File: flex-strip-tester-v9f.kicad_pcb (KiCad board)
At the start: 2 copper layers, 68.8 x 11.1 mm, 12 parts, among them J2 Conn_01x01_Female

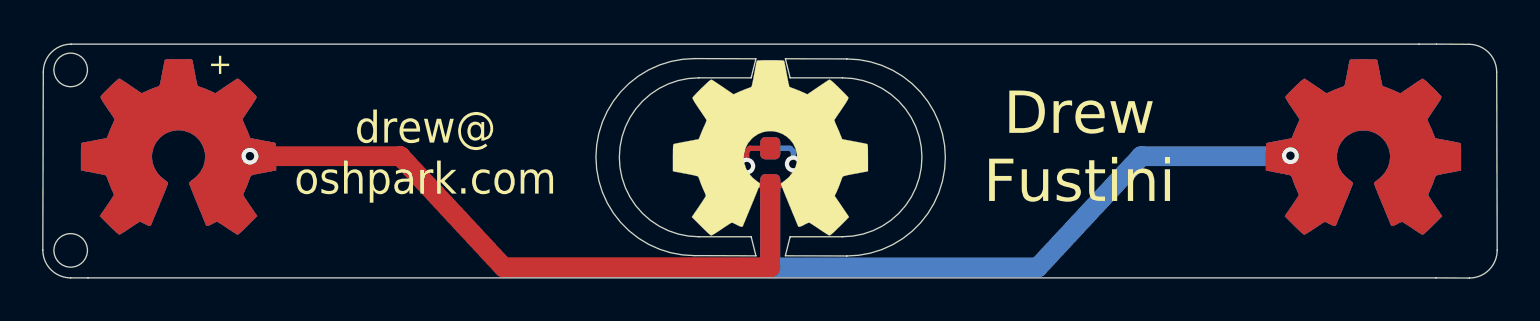
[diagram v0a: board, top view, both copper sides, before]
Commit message: add v10 which is being order from oshpark flex
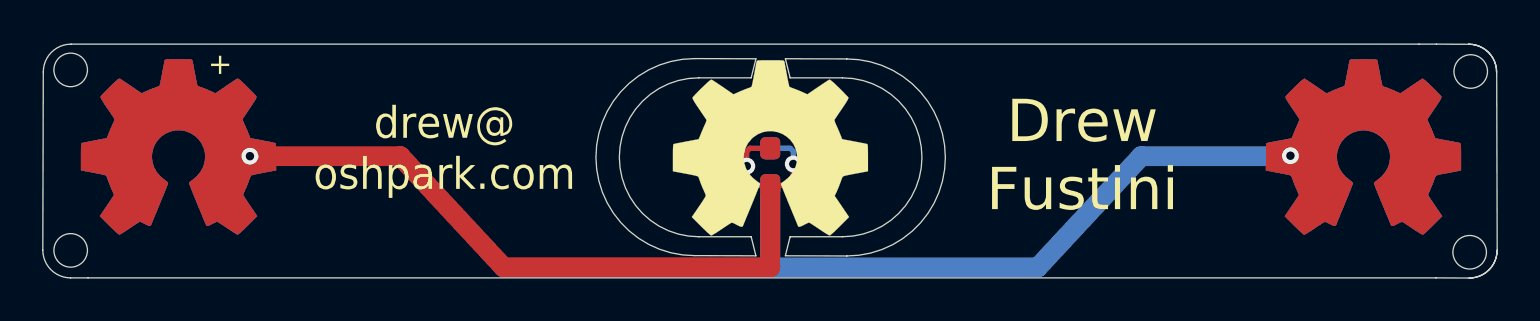
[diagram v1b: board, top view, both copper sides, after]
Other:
- outline, holes or cut-outs redrawn
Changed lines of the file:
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@@
-(kicad_pcb (version 20200628) (host pcbnew "(5.99.0-2143-g1463dd10b)")
+(kicad_pcb (version 20200628) (host pcbnew "(5.99.0-2281-g2f31bf278-dirty)")
   (general
     (thickness 0.1)
-    (drawings 85)
+    (drawings 89)
     (tracks 24)
     (modules 12)
@@
     )
   )
+  (gr_arc (start 186.273635 99.979326) (end 186.273635 101.29404) (angle -90) (layer "Edge.Cuts") (width 0.05))
+  (gr_circle (center 186.293095 100.075) (end 186.883095 100.605) (layer "Edge.Cuts") (width 0.05))
+  (gr_arc (start 186.247423 91.54446) (end 187.562137 91.54446) (angle -90) (layer "Edge.Cuts") (width 0.05))
+  (gr_circle (center 186.343097 91.525) (end 186.873097 90.935) (layer "Edge.Cuts") (width 0.05))
   (gr_line (start 152.5325 90.924712) (end 149.625 90.914904) (layer "Edge.Cuts") (width 0.05))
   (gr_line (start 152.3075 91.825096) (end 149.83 91.825096) (layer "Edge.Cuts") (width 0.05))
@@
   (gr_line (start 153.23 95.43) (end 187.57 95.43) (layer "F.Fab") (width 0.1))
   (gr_line (start 146.06 100.83) (end 186.9286 100.83) (layer "B.Fab") (width 0.1))
-  (gr_text "Drew\nFustini" (at 167.83558 95.11284) (layer "F.SilkS")
+  (gr_text "Drew\nFustini" (at 167.975 95.5) (layer "F.SilkS")
     (effects (font (size 2 2) (thickness 0.3)))
   )
@@
   (gr_line (start 155.2575 99.06) (end 154.6225 99.06) (layer "Eco1.User") (width 0.1))
   (gr_line (start 154.6225 99.06) (end 154.6225 98.3615) (layer "Eco1.User") (width 0.1))
-  (gr_text "drew@\noshpark.com" (at 136.9 95.4) (layer "F.SilkS")
+  (gr_text "drew@\noshpark.com" (at 137.8 95.175) (layer "F.SilkS")
     (effects (font (size 1.5 1.4) (thickness 0.2)))
   )
-  (gr_text "github.com/\noshpark/\nflextester" (at 136.4 95.5) (layer "B.SilkS")
+  (gr_text "github.com/\noshpark/\nflextester" (at 137.625 95.3) (layer "B.SilkS")
     (effects (font (size 1.5 1.5) (thickness 0.2286)) (justify mirror))
   )
@@
     (effects (font (size 1 1) (thickness 0.15)))
   )
-  (gr_text "Flex\nbattery \ntester" (at 168.00322 95.76054) (layer "B.SilkS")
+  (gr_text "Flex\nbattery \ntester" (at 168.45 95.55) (layer "B.SilkS")
     (effects (font (size 1.5 1.5) (thickness 0.2286)) (justify mirror))
   )
